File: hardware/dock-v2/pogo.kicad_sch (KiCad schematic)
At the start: 17 parts, among them J601 Pogo 7-pin, Q601 2N7002, Q602 2N7002, U601 TPD4E1U06DBVR, U602 SY6280AAC

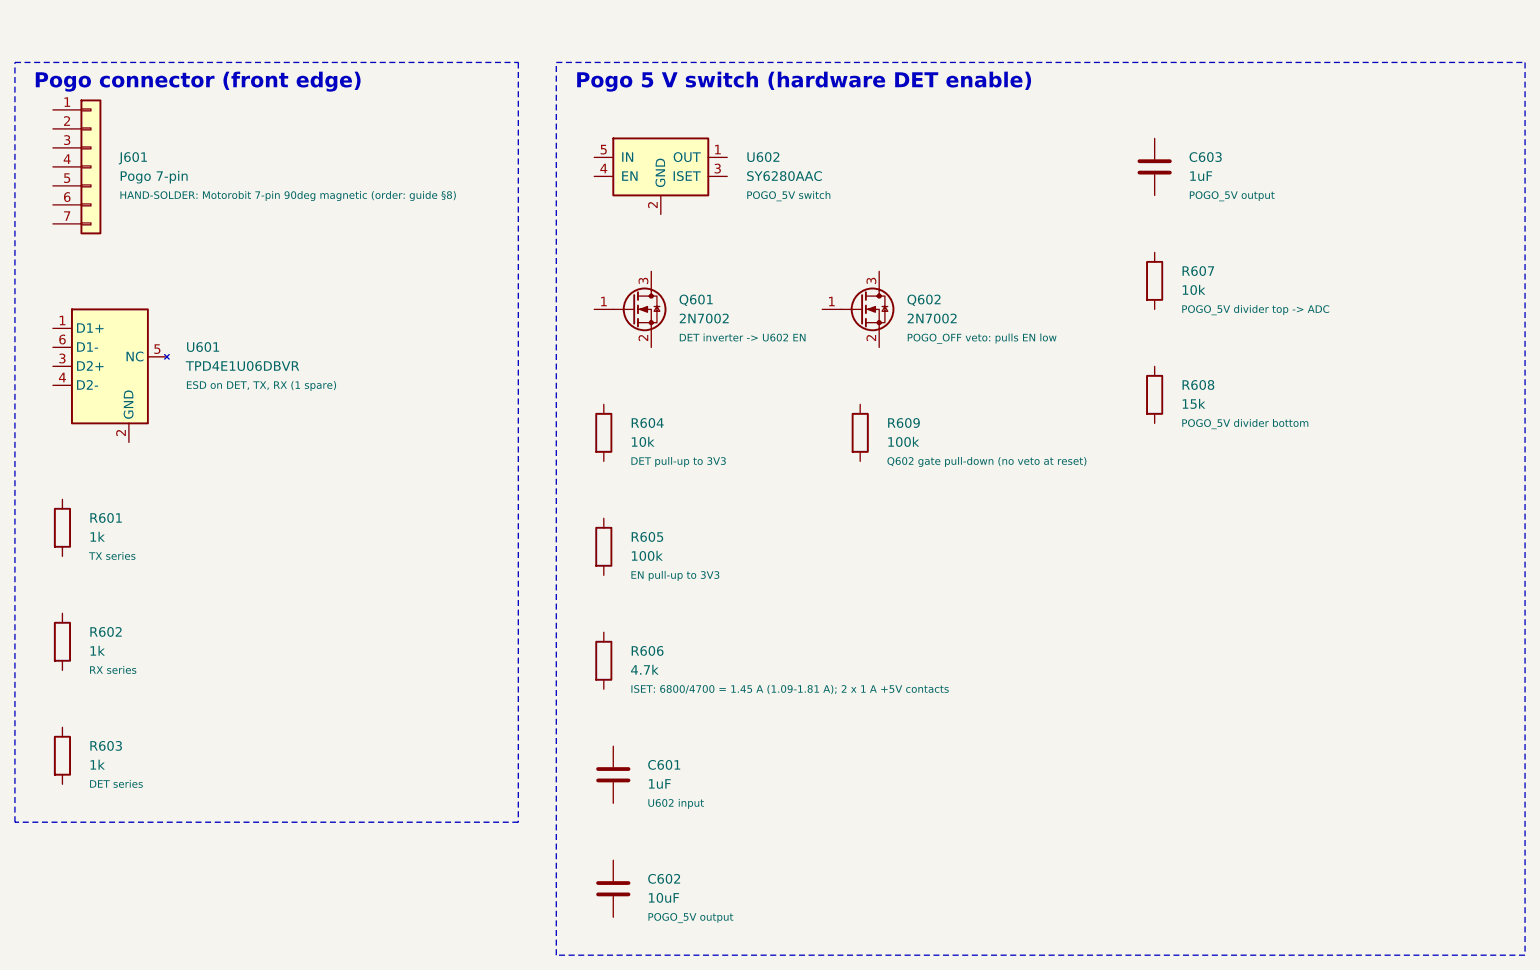
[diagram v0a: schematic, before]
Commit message: Dock v2 schematic: pogo sheet wired, fixes from review (user's work, snapshot)
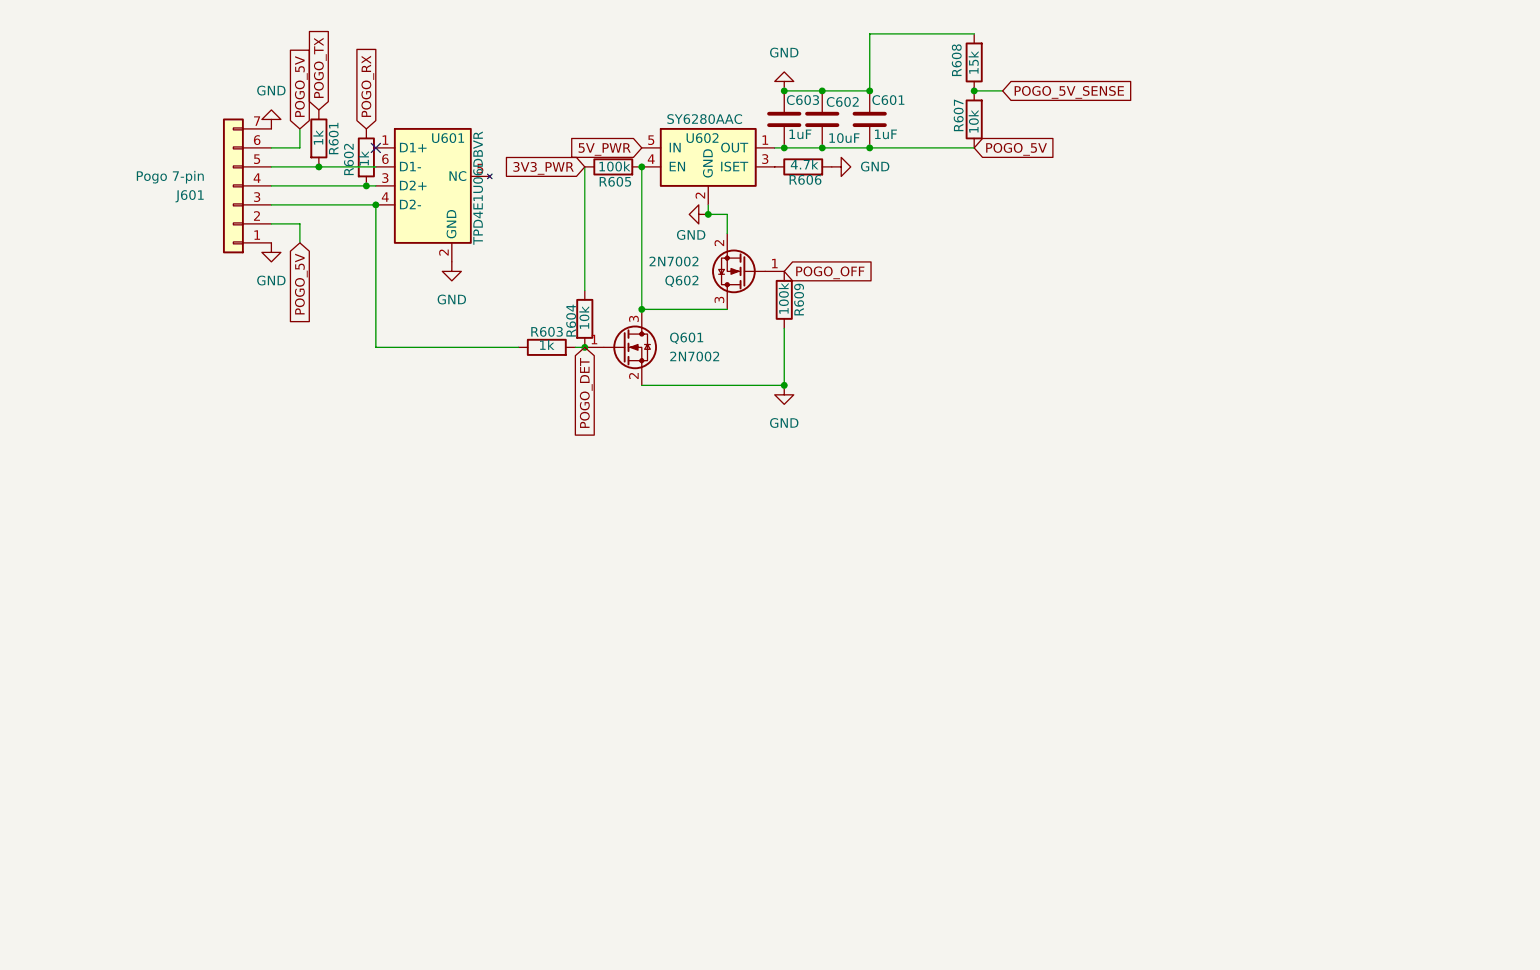
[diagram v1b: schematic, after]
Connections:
- net POGO_OFF: now reaches Q602.1 (G)
- net POGO_OFF: now also R609.2
- net GND: now reaches Q602.2 (S)
- net GND: now also C601.1, C602.1, C603.1, J601.1 (Pin_1), J601.7 (Pin_7), Q601.2 (S), R606.2, R608.2, R609.1, U601.2 (GND), U602.2 (GND)
- net at Q602.3 (D): now also Q601.3 (D), R605.2, U602.4 (EN)
- net POGO_RX: now reaches R602.1
- net at R602.2: now also J601.4 (Pin_4), U601.3 (D2+)
- net POGO_5V: now reaches C601.2
- net POGO_5V: now also C602.2, C603.2, J601.2 (Pin_2), J601.6 (Pin_6), R607.1, U602.1 (OUT)
- net 3V3_PWR: now reaches R604.1
- net 3V3_PWR: now also R605.1
- net POGO_DET: now reaches R604.2
- net POGO_DET: now also Q601.1 (G), R603.2
- net at R603.1: now also J601.3 (Pin_3), U601.4 (D2-)
- net POGO_5V_SENSE: now reaches R607.2
- net POGO_5V_SENSE: now also R608.1
- net at R606.1: now also U602.3 (ISET)
- net at U601.6 (D1-): now also J601.5 (Pin_5), R601.2
- net POGO_TX: now reaches R601.1
- net 5V_PWR: now reaches U602.5 (IN)
- no-connect marks 0 -> 1
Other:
- note removed: "Pogo 5 V switch (hardware DET enable)"
- note removed: "Pogo connector (front edge)"
- moved on the sheet: C601, C602, C603, J601, Q601, Q602, R601, R602, R603, R604, R605, R606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

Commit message: Dock v2 schematic: user's fixes (snapshot)
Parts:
- removed C603: 1uF, Capacitor_SMD:C_0402_1005Metric, symbol Device:C
- added C601: 1uF, Capacitor_SMD:C_0402_1005Metric, symbol Device:C
- renumbered C601 to C603
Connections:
- net 5V_PWR: now also C601.2
- net GND: now also C601.1
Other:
- moved on the sheet: C602, C603, R607, R608

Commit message: Dock v2: placement and partial routing (user's work, snapshot)
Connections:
- net at J601.4 (Pin_4), R602.2: now also U601.4 (D2-); no longer U601.3 (D2+)
- net at J601.3 (Pin_3), R603.1: now also U601.3 (D2+); no longer U601.4 (D2-)
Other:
- moved on the sheet: R602
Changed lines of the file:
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@@
+	)
+	(junction
+		(at 114.3 21.59)
+		(diameter 0)
+		(color 0 0 0 0)
+	)
+	(junction
+		(at 114.3 29.21)
+		(diameter 0)
+		(color 0 0 0 0)
+	)
+	(junction
+		(at 129.54 21.59)
+		(diameter 0)
+		(color 0 0 0 0)
+	)
+	(junction
+		(at 57.15 36.83)
+		(diameter 0)
+		(color 0 0 0 0)
+	)
+	(junction
+		(at 115.57 60.96)
+		(diameter 0)
+		(color 0 0 0 0)
 	)
 	(junction
@@
 	)
 	(junction
-		(at 114.3 21.59)
-		(diameter 0)
-		(color 0 0 0 0)
-	)
-	(junction
-		(at 114.3 29.21)
-		(diameter 0)
-		(color 0 0 0 0)
-	)
-	(junction
-		(at 129.54 21.59)
-		(diameter 0)
-		(color 0 0 0 0)
-	)
-	(junction
-		(at 115.57 60.96)
-		(diameter 0)
-		(color 0 0 0 0)
-	)
-	(junction
 		(at 88.9 55.88)
 		(diameter 0)
@@
 	)
 	(junction
-		(at 59.69 34.29)
+		(at 59.69 38.1)
 		(diameter 0)
 		(color 0 0 0 0)
@@
 	(wire
 		(pts
+			(xy 57.15 29.21) (xy 58.42 26.67)
+		)
+		(stroke
+			(width 0)
+			(type default)
+		)
+	)
+	(wire
+		(pts
 			(xy 87.63 55.88) (xy 88.9 55.88)
 		)
@@
 	(wire
 		(pts
+			(xy 59.69 38.1) (xy 59.69 34.29)
+		)
+		(stroke
+			(width 0)
+			(type default)
+		)
+	)
+	(wire
+		(pts
 			(xy 105.41 38.1) (xy 105.41 36.83)
 		)
@@
 	(wire
 		(pts
+			(xy 50.8 34.29) (xy 46.99 34.29)
+		)
+		(stroke
+			(width 0)
+			(type default)
+		)
+	)
+	(wire
+		(pts
 			(xy 88.9 31.75) (xy 88.9 48.26)
 		)
@@
 	(wire
 		(pts
-			(xy 60.96 55.88) (xy 80.01 55.88)
+			(xy 49.53 38.1) (xy 59.69 38.1)
 		)
 		(stroke
@@
 	(wire
 		(pts
-			(xy 60.96 36.83) (xy 60.96 55.88)
+			(xy 59.69 34.29) (xy 60.96 34.29)
+		)
+		(stroke
+			(width 0)
+			(type default)
+		)
+	)
+	(wire
+		(pts
+			(xy 50.8 36.83) (xy 50.8 34.29)
 		)
 		(stroke
@@
 	(wire
 		(pts
-			(xy 46.99 34.29) (xy 59.69 34.29)
-		)
-		(stroke
-			(width 0)
-			(type default)
-		)
-	)
-	(wire
-		(pts
 			(xy 114.3 21.59) (xy 120.65 21.59)
 		)
@@
 	(wire
 		(pts
-			(xy 59.69 34.29) (xy 60.96 34.29)
+			(xy 57.15 36.83) (xy 60.96 36.83)
 		)
 		(stroke
@@
 	(wire
 		(pts
+			(xy 46.99 36.83) (xy 49.53 36.83)
+		)
+		(stroke
+			(width 0)
+			(type default)
+		)
+	)
+	(wire
+		(pts
 			(xy 133.35 21.59) (xy 129.54 21.59)
 		)
@@
 	(wire
 		(pts
+			(xy 59.69 55.88) (xy 80.01 55.88)
+		)
+		(stroke
+			(width 0)
+			(type default)
+		)
+	)
+	(wire
+		(pts
+			(xy 50.8 36.83) (xy 57.15 36.83)
+		)
+		(stroke
+			(width 0)
+			(type default)
+		)
+	)
+	(wire
+		(pts
+			(xy 49.53 36.83) (xy 49.53 38.1)
+		)
+		(stroke
+			(width 0)
+			(type default)
+		)
+	)
+	(wire
+		(pts
 			(xy 50.8 41.91) (xy 50.8 39.37)
 		)
@@
 	(wire
 		(pts
+			(xy 59.69 38.1) (xy 59.69 55.88)
+		)
+		(stroke
+			(width 0)
+			(type default)
+		)
+	)
+	(wire
+		(pts
 			(xy 129.54 13.97) (xy 120.65 13.97)
 		)
@@
 	(wire
 		(pts
-			(xy 46.99 36.83) (xy 60.96 36.83)
+			(xy 63.5 36.83) (xy 60.96 36.83)
 		)
 		(stroke
@@
 	(global_label "POGO_RX"
 		(shape input)
-		(at 59.69 26.67 90)
+		(at 58.42 26.67 90)
 		(fields_autoplaced yes)
 		(effects
@@
 		)
 		(property "Intersheetrefs" "${INTERSHEET_REFS}"
-			(at 59.69 15.0367 90)
+			(at 58.42 15.0367 90)
 			(hide yes)
 			(show_name no)
@@
 	(symbol
 		(lib_id "Device:R")
-		(at 59.69 30.48 0)
+		(at 57.15 33.02 0)
 		(unit 1)
 		(body_style 1)
@@
 		(dnp no)
 		(property "Reference" "R602"
-			(at 57.404 33.02 90)
+			(at 54.864 35.56 90)
 			(show_name no)
 			(do_not_autoplace no)
@@
 		)
 		(property "Value" "1k"
-			(at 59.436 31.75 90)
+			(at 56.896 34.29 90)
 			(show_name no)
 			(do_not_autoplace no)
@@
 		)
 		(property "Footprint" "Resistor_SMD:R_0402_1005Metric"
-			(at 59.69 30.48 0)
+			(at 57.15 33.02 0)
 			(hide yes)
 			(show_name no)
@@
 		)
 		(property "Datasheet" ""
-			(at 59.69 30.48 0)
+			(at 57.15 33.02 0)
 			(hide yes)
 			(show_name no)
@@
 		)
 		(property "Description" "Resistor"
-			(at 59.69 30.48 0)
+			(at 57.15 33.02 0)
 			(hide yes)
 			(show_name no)
@@
 		)
 		(property "LCSC" "C11702"
-			(at 59.69 30.48 0)
+			(at 57.15 33.02 0)
 			(hide yes)
 			(show_name no)
@@
 		)
 		(property "Note" "RX series"
-			(at 63.25 34.29 0)
-			(hide yes)
-			(show_name no)
+			(at 60.71 36.83 0)
+			(hide yes)
+			(show_name no)
